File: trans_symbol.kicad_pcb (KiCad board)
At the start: 2 copper layers, 81.7 x 93.6 mm, 100 parts, among them J4 Conn_01x04, SW1 SW_SPST, U1 ATSAMD21G18A-AU, U2 MIC5504-3.3YM5, Y1 32768Hz

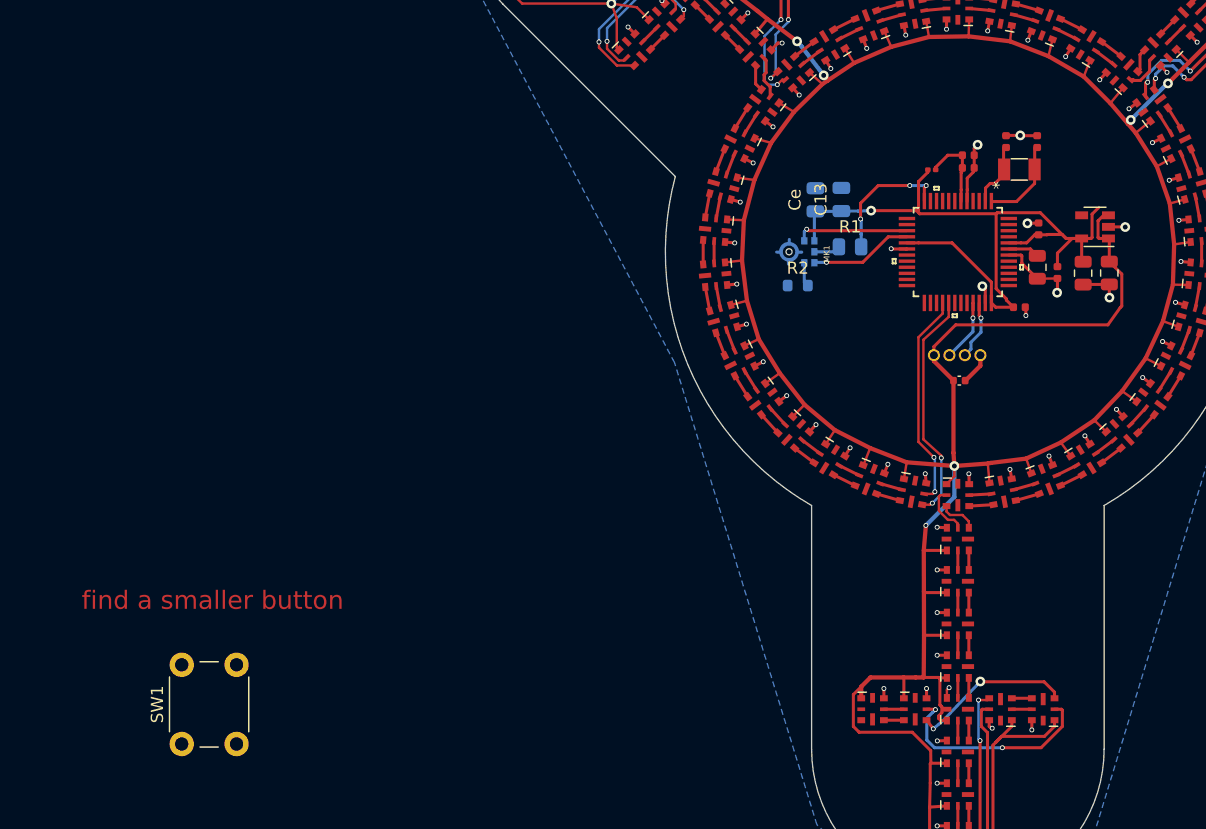
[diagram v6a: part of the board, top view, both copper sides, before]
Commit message: add three buttons; untested beacuse I've bricked my samd board again, trying to get it to come back alive
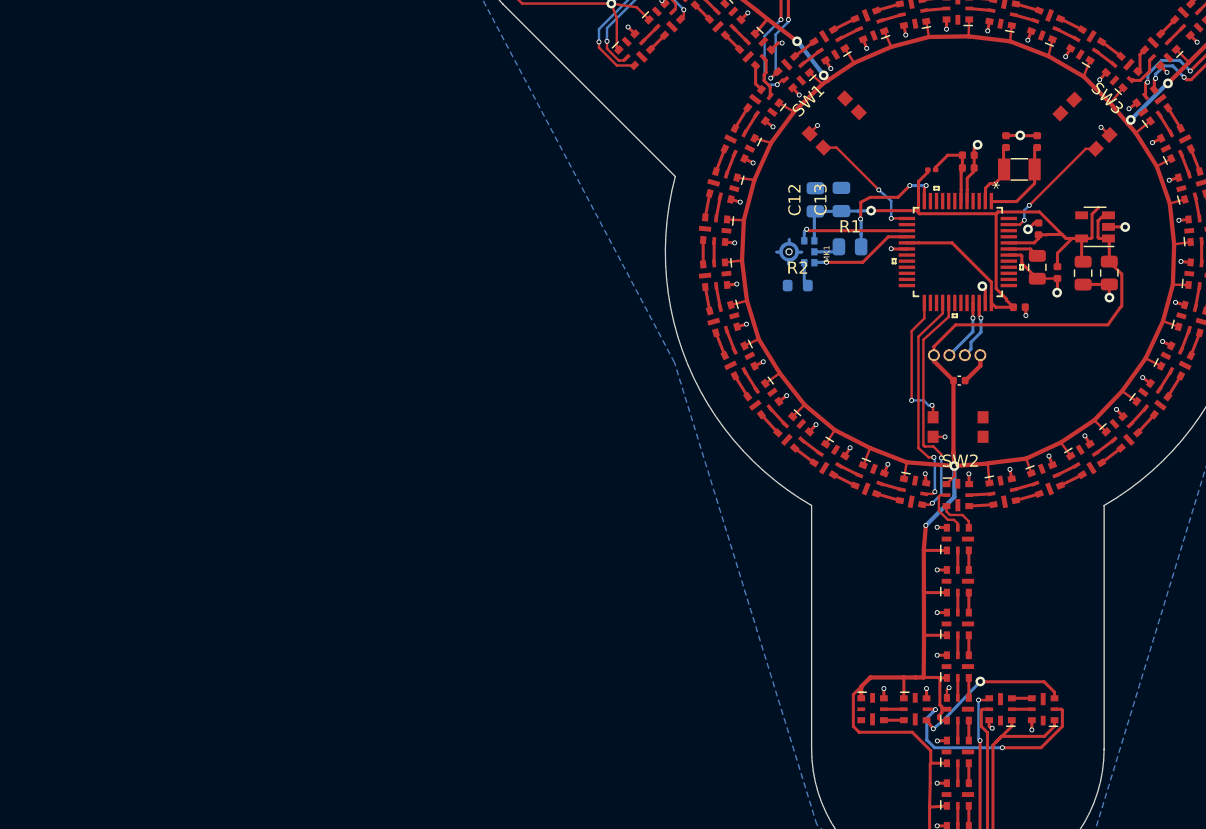
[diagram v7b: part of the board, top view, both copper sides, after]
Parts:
- added SW2: SW_SPST, Button_Switch_SMD:KMR731NG LFS (opal), F.Cu at (90.0, 104.3)
- added SW3: SW_SPST, Button_Switch_SMD:KMR731NG LFS (opal), F.Cu at (100.4, 79.5)
- SW1: footprint Button_Switch_THT:SW_PUSH_6mm_H5mm -> Button_Switch_SMD:KMR731NG LFS (opal)
- moved SW1 73.9 mm to (79.9, 79.4), turned to 225 degrees
- renumbered Ce to C12
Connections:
- SW1 pad 1: Net-(SW1-Pad1) -> BUTTON_1
- SW1 pad 2: Net-(SW1-Pad2) -> GND
- U1 pad 13: Net-(U1-Pad13) -> BUTTON_1
- U1 pad 25: Net-(U1-Pad25) -> BUTTON_2
- U1 pad 47: Net-(U1-Pad47) -> BUTTON_3
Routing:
- net BUTTON_2: track 0.00 -> 11.3 mm, vias 0 -> 2
- net BUTTON_3: track 0.00 -> 10.2 mm, vias 0 -> 2
- net BUTTON_1: track 0.00 -> 10.1 mm, vias 0 -> 2
- net GND: track 89.6 -> 92.8 mm, vias 86 -> 89
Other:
- board text removed: "find a smaller button"
